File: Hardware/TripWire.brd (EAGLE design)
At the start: 32.3 x 50.2 mm, 56 parts, among them P1 LSP11, P2 LSP11, P3 LSP11, P4 LSP11, P5 LSP11, P6 LSP11, P7 LSP11, X1 GADGETEER-SOCKET

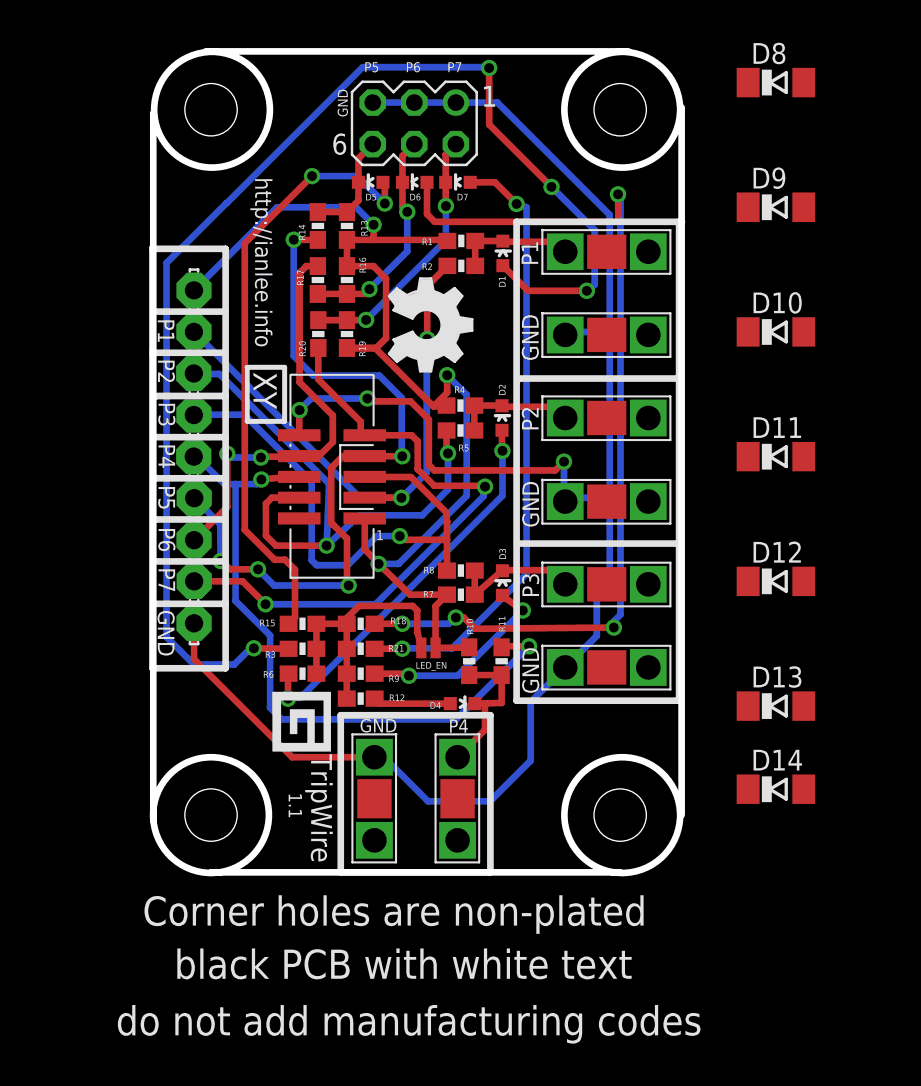
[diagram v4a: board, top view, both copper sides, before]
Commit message: WiP - adding TVS diode array.
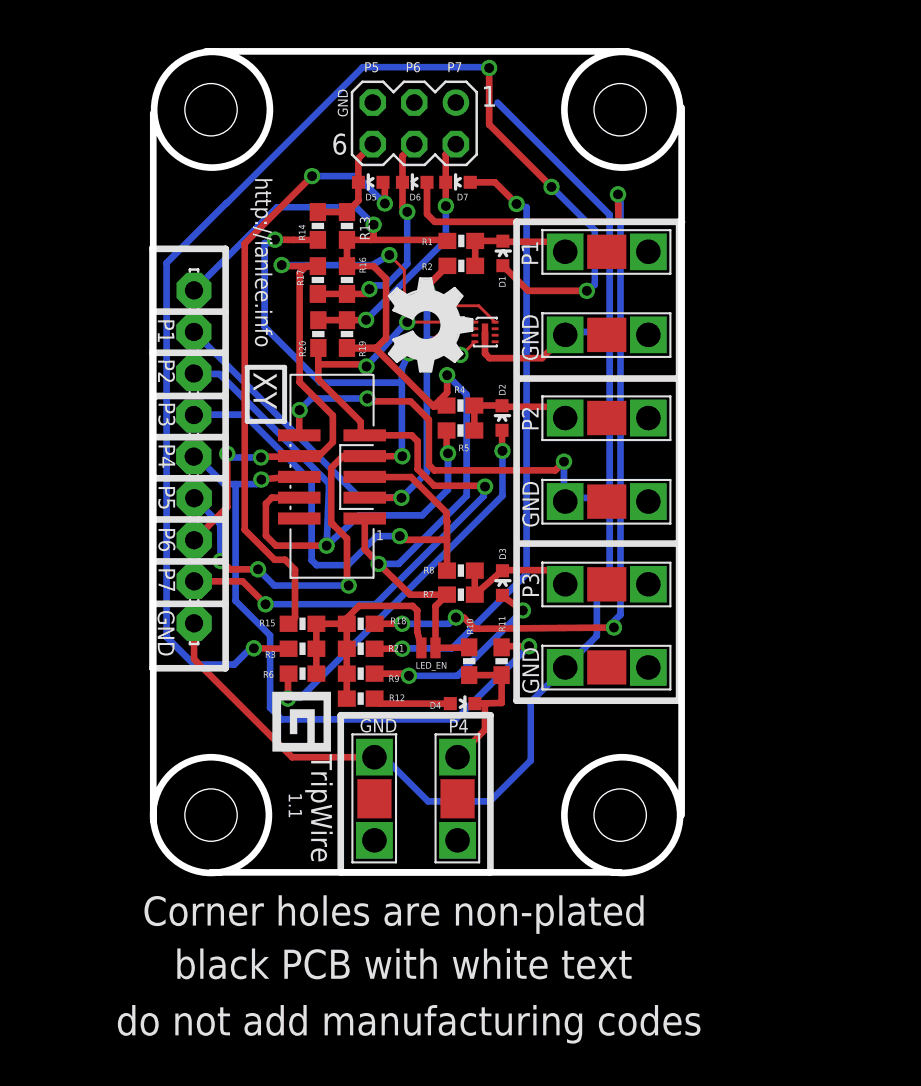
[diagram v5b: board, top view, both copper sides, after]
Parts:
- removed D10, D11, D12, D13, D14, D8, D9: (no value), diode:SOD80C
- added VESD05A8A-HNH-GS08: VESD05A8A-HNH-GS088-UFDFN_TVS-DIODE-ARRAY, SoftDust:8-UFDFN
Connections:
- removed net N$15: D9.A
- removed net N$16: D10.A
- net GND: now also VESD05A8A-HNH-GS08.P$9; no longer D11.A, D12.A, D13.A, D14.A, D8.A
- net PIN3: now also VESD05A8A-HNH-GS08.P$4; no longer D11.C
- net PIN4: now also VESD05A8A-HNH-GS08.P$6; no longer D13.C
- net PIN5: now also VESD05A8A-HNH-GS08.P$3; no longer D12.C
- net PIN6: now also VESD05A8A-HNH-GS08.P$7; no longer D14.C
- net PIN7: now also VESD05A8A-HNH-GS08.P$2; no longer D8.C
- net PIN8: now also VESD05A8A-HNH-GS08.P$8; no longer D9.C
- net PIN9: now also VESD05A8A-HNH-GS08.P$1; no longer D10.C
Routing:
- net PIN8: track 24.2 -> 42.1 mm, vias 2 -> 4
- net PIN9: track 37.8 -> 48.6 mm, vias 2 -> 4
- net PIN7: track 45.0 -> 54.3 mm, vias 5 -> 6
- net PIN3: track 34.5 -> 38.1 mm, vias 2 -> 3
- net GND: track 109.4 -> 108.7 mm

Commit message: Adjusted text sizes & placement.
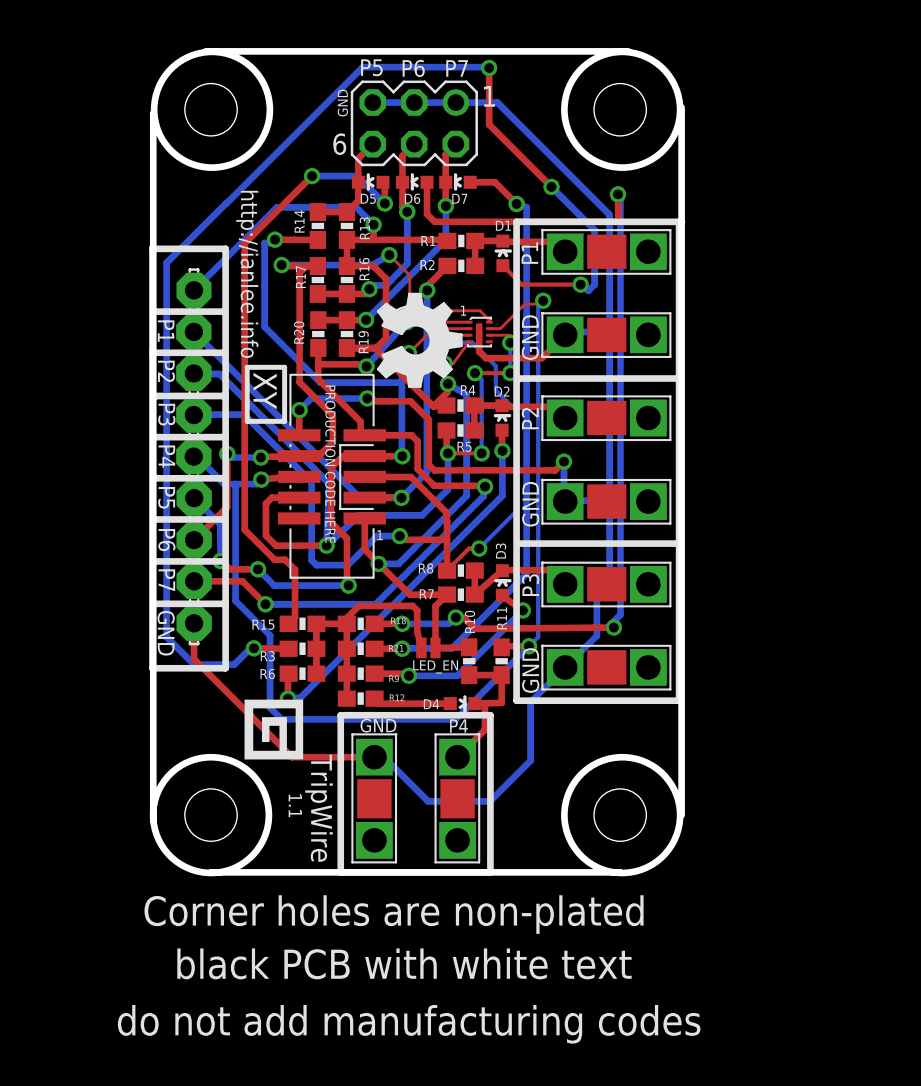
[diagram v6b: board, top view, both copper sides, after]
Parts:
- D1, D2, D3, D4, D5, D6, D7: value (none) -> Green 10mA
- SV1: value (none) -> Header
- moved LOGO1 1.15 mm to (13.8, 35.3)
- moved VESD05A8A-HNH-GS08 0.36 mm to (20.0, 33.0)
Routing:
- net PIN6: track 41.6 -> 67.0 mm, vias 2 -> 3
- net PIN5: track 32.4 -> 53.1 mm, vias 1 -> 3
- net PIN4: track 35.4 -> 48.3 mm, vias 2 -> 6
- net GND: track 108.7 -> 117.0 mm
- net PIN8: track 42.1 -> 44.4 mm
- net 3V3: track 69.7 -> 68.8 mm
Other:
- board text added: "PRODUCTION CODE HERE"
